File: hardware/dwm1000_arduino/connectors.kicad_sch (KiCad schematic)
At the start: 10 parts, among them J1 Barrel_Jack, J2 PWR_IN, J3 UART, J4 SPI, J5 NEO_OUT, J6 Conn_01x06_Male

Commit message: finixh schematic and first pass layout
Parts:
- removed J1: Barrel_Jack, symbol Connector:Barrel_Jack
- removed J2: PWR_IN, symbol Connector:Screw_Terminal_01x03
- added J1: RAW_PWR, TerminalBlock_Phoenix:TerminalBlock_Phoenix_PT-1,5-2-3.5-H_1x02_P3.50mm_Horizontal, symbol Connector:Screw_Terminal_01x02
- added J2: PWR_IN, TerminalBlock_Phoenix:TerminalBlock_Phoenix_PT-1,5-4-3.5-H_1x04_P3.50mm_Horizontal, symbol Connector:Screw_Terminal_01x04
- F1, F2: footprint (none) -> Fuse:Fuse_1206_3216Metric_Pad1.42x1.75mm_HandSolder; DigiKey (none) -> 507-1802-6-ND
- J3, J4: footprint (none) -> TerminalBlock_Phoenix:TerminalBlock_Phoenix_PT-1,5-4-3.5-H_1x04_P3.50mm_Horizontal; DigiKey (none) -> 277-1860-ND
- J5: footprint (none) -> Connector_PinHeader_2.54mm:PinHeader_1x03_P2.54mm_Vertical
- J6: value Conn_01x06_Male -> DEBUG; footprint (none) -> Connector_PinHeader_2.54mm:PinHeader_1x06_P2.54mm_Vertical
- TP1, TP2: footprint (none) -> TestPoint:TestPoint_Pad_D2.5mm
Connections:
- net ARD_RX: now also J3.2 (Pin_2); no longer J3.1 (Pin_1)
- net ARD_TX: now also J3.1 (Pin_1); no longer J3.2 (Pin_2)
- net GND: now also J1.1 (Pin_1), J2.1 (Pin_1), J2.2 (Pin_2)
- net SPI_MISO: now also J4.4 (Pin_4); no longer J4.3 (Pin_3)
- net SPI_MOSI: now also J4.3 (Pin_3); no longer J4.4 (Pin_4)
- net VCC: now also J1.2 (Pin_2)
- net at F2.1: now also J2.3 (Pin_3)
- net at F1.1: now also J2.4 (Pin_4)

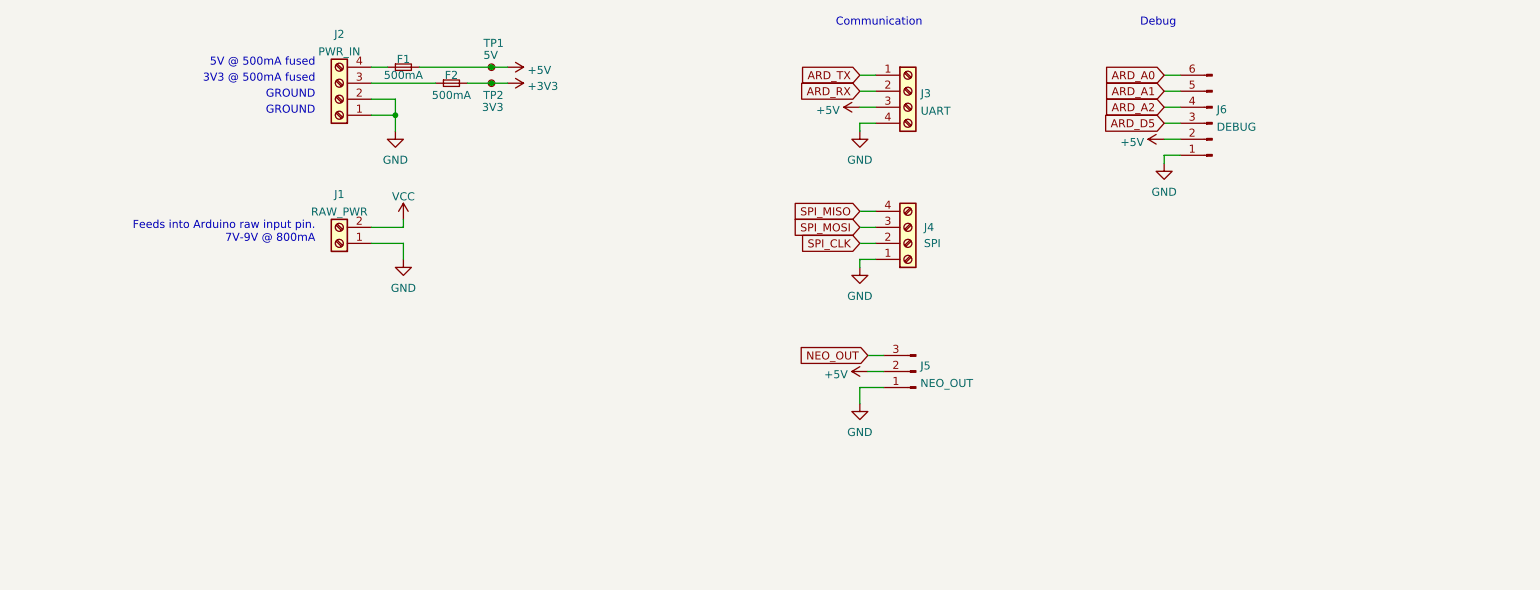
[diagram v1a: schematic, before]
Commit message: start rev 2 of the dwm board
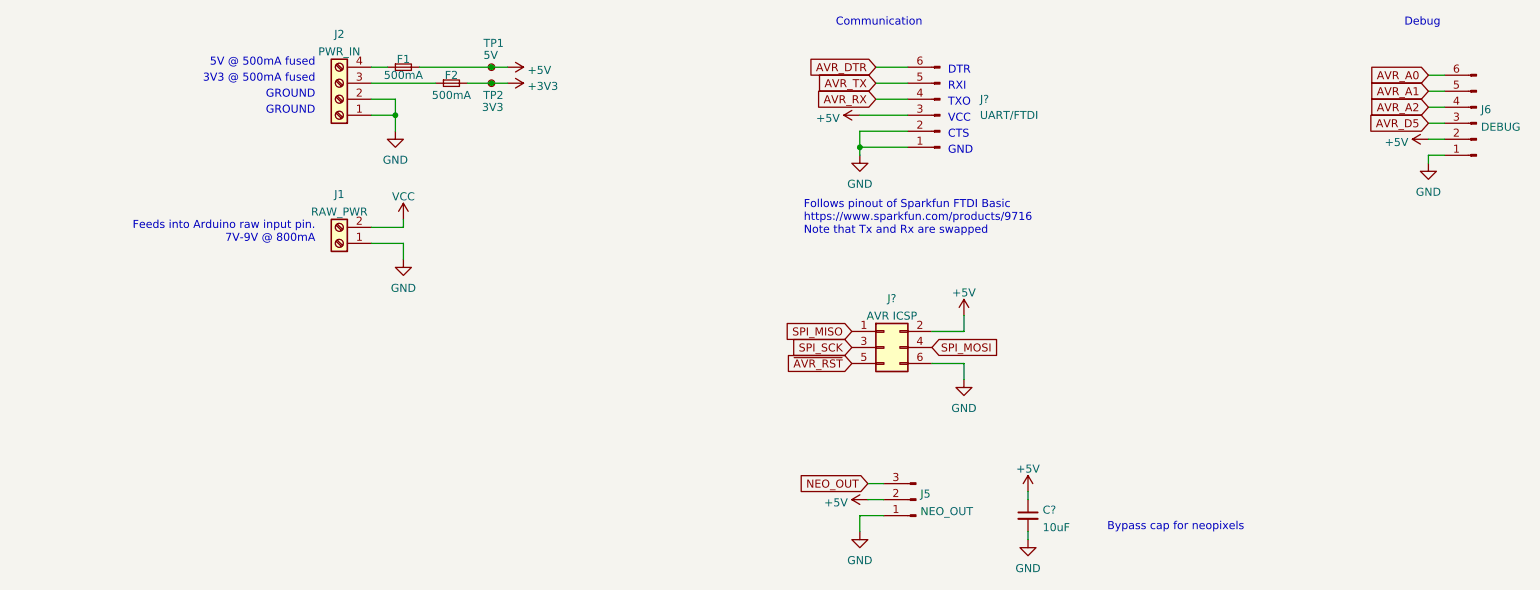
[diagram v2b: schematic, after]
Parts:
- removed J3: UART, TerminalBlock_Phoenix:TerminalBlock_Phoenix_PT-1,5-4-3.5-H_1x04_P3.50mm_Horizontal, symbol Connector:Screw_Terminal_01x04
- removed J4: SPI, TerminalBlock_Phoenix:TerminalBlock_Phoenix_PT-1,5-4-3.5-H_1x04_P3.50mm_Horizontal, symbol Connector:Screw_Terminal_01x04
- added C?: 10uF, Capacitor_SMD:C_0805_2012Metric_Pad1.18x1.45mm_HandSolder, symbol Device:C_Small
- added J?: UART/FTDI, Connector_PinHeader_2.54mm:PinHeader_1x06_P2.54mm_Vertical, symbol Connector:Conn_01x06_Male
- added J?: AVR ICSP, symbol Connector_Generic:Conn_02x03_Odd_Even
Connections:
- net +5V: now also C?.1, J?.2 (Pin_2), J?.3 (Pin_3)
- net GND: now also C?.2, J?.1 (Pin_1), J?.2 (Pin_2), J?.6 (Pin_6)
- net SPI_MISO: now also J?.1 (Pin_1)
- net SPI_MOSI: now also J?.4 (Pin_4)
- net ARD_A0 renamed AVR_A0
- net ARD_A1 renamed AVR_A1
- net ARD_A2 renamed AVR_A2
- net ARD_D5 renamed AVR_D5
- new net AVR_DTR: J?.6 (Pin_6)
- new net AVR_RX: J?.4 (Pin_4)
- new net AVR_TX: J?.5 (Pin_5)
- new net SPI_SCK: J?.3 (Pin_3)
- new net ~{AVR_RST}: J?.5 (Pin_5)
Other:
- note added: "Bypass cap for neopixels"
- note added: "CTS"
- note added: "DTR"
- note added: "Follows pinout of Sparkfun FTDI Basic https://www.sparkfun.com/products/9716 Note that Tx and Rx are swapped"
- note added: "GND"
- note added: "RXI"
- note added: "TXO"
- note added: "VCC"
- moved on the sheet: J5, J6

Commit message: rev 2 pcb schematic
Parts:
- gave numbers to parts that had none: 3
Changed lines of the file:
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@@
   (symbol (lib_id "power:GND") (at 199.39 148.59 0) (unit 1)
     (in_bom yes) (on_board yes) (fields_autoplaced)
-    (property "Reference" "#PWR?" (id 0) (at 199.39 154.94 0)
+    (property "Reference" "#PWR044" (id 0) (at 199.39 154.94 0)
       (effects (font (size 1.27 1.27)) hide)
     )
@@
   (symbol (lib_id "power:+5V") (at 199.39 138.43 0) (unit 1)
     (in_bom yes) (on_board yes) (fields_autoplaced)
-    (property "Reference" "#PWR?" (id 0) (at 199.39 142.24 0)
+    (property "Reference" "#PWR043" (id 0) (at 199.39 142.24 0)
       (effects (font (size 1.27 1.27)) hide)
     )
@@
   (symbol (lib_id "Connector:Conn_01x06_Male") (at 195.58 106.68 180) (unit 1)
     (in_bom yes) (on_board yes)
-    (property "Reference" "J?" (id 0) (at 201.93 104.14 0)
+    (property "Reference" "J4" (id 0) (at 201.93 104.14 0)
       (effects (font (size 1.27 1.27)) (justify right))
     )
@@
   (symbol (lib_id "power:+5V") (at 209.55 166.37 0) (unit 1)
     (in_bom yes) (on_board yes) (fields_autoplaced)
-    (property "Reference" "#PWR?" (id 0) (at 209.55 170.18 0)
+    (property "Reference" "#PWR045" (id 0) (at 209.55 170.18 0)
       (effects (font (size 1.27 1.27)) hide)
     )
@@
   (symbol (lib_id "Device:C_Small") (at 209.55 170.18 0) (unit 1)
     (in_bom yes) (on_board yes) (fields_autoplaced)
-    (property "Reference" "C?" (id 0) (at 211.8741 169.2778 0)
+    (property "Reference" "C15" (id 0) (at 211.8741 169.2778 0)
       (effects (font (size 1.27 1.27)) (justify left))
     )
@@
   (symbol (lib_id "power:GND") (at 209.55 173.99 0) (unit 1)
     (in_bom yes) (on_board yes) (fields_autoplaced)
-    (property "Reference" "#PWR?" (id 0) (at 209.55 180.34 0)
+    (property "Reference" "#PWR046" (id 0) (at 209.55 180.34 0)
       (effects (font (size 1.27 1.27)) hide)
     )
@@
   (symbol (lib_id "Connector_Generic:Conn_02x03_Odd_Even") (at 186.69 143.51 0) (unit 1)
     (in_bom yes) (on_board yes) (fields_autoplaced)
-    (property "Reference" "J?" (id 0) (at 187.96 135.7335 0))
+    (property "Reference" "J3" (id 0) (at 187.96 135.7335 0))
     (property "Value" "AVR ICSP" (id 1) (at 187.96 138.5086 0))
     (property "Footprint" "" (id 2) (at 186.69 143.51 0)

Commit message: finish layout
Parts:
- J2: value PWR_IN -> PWR_OUT
- J3: footprint (none) -> Connector_PinHeader_2.54mm:PinHeader_2x03_P2.54mm_Vertical
- TP1, TP2: footprint TestPoint:TestPoint_Pad_D2.5mm -> TestPoint:TestPoint_Pad_D1.0mm
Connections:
- net NEO_OUT renamed NEO_DATA
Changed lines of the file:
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@@
     (effects (font (size 1.27 1.27)) (justify left bottom))
   )
-  (global_label "NEO_OUT" (shape input) (at 184.15 165.1 180) (fields_autoplaced)
-    (effects (font (size 1.27 1.27)) (justify right))
-    (property "Intersheet References" "${INTERSHEET_REFS}" (id 0) (at 173.3307 165.0206 0)
+  (global_label "NEO_DATA" (shape input) (at 184.15 165.1 180) (fields_autoplaced)
+    (effects (font (size 1.27 1.27)) (justify right))
+    (property "Intersheet References" "${INTERSHEET_REFS}" (id 0) (at 172.5445 165.0206 0)
       (effects (font (size 1.27 1.27)) (justify right) hide)
     )
@@
     (in_bom yes) (on_board yes) (fields_autoplaced)
     (property "Reference" "J2" (id 0) (at 100.33 93.8235 0))
-    (property "Value" "PWR_IN" (id 1) (at 100.33 96.5986 0))
+    (property "Value" "PWR_OUT" (id 1) (at 100.33 96.5986 0))
     (property "Footprint" "TerminalBlock_Phoenix:TerminalBlock_Phoenix_PT-1,5-4-3.5-H_1x04_P3.50mm_Horizontal" (id 2) (at 100.33 104.14 0)
       (effects (font (size 1.27 1.27)) hide)
@@
       (effects (font (size 1.27 1.27)) (justify left))
     )
-    (property "Footprint" "TestPoint:TestPoint_Pad_D2.5mm" (id 2) (at 119.38 101.6 0)
+    (property "Footprint" "TestPoint:TestPoint_Pad_D1.0mm" (id 2) (at 119.38 101.6 0)
       (effects (font (size 1.27 1.27)) hide)
     )
@@
     (property "Reference" "J3" (id 0) (at 187.96 135.7335 0))
     (property "Value" "AVR ICSP" (id 1) (at 187.96 138.5086 0))
-    (property "Footprint" "" (id 2) (at 186.69 143.51 0)
+    (property "Footprint" "Connector_PinHeader_2.54mm:PinHeader_2x03_P2.54mm_Vertical" (id 2) (at 186.69 143.51 0)
       (effects (font (size 1.27 1.27)) hide)
     )
@@
       (effects (font (size 1.27 1.27)) (justify left))
     )
-    (property "Footprint" "TestPoint:TestPoint_Pad_D2.5mm" (id 2) (at 129.54 99.06 0)
-      (effects (font (size 1.27 1.27)) hide)
-    )
+    (property "Footprint" "TestPoint:TestPoint_Pad_D1.0mm" (id 2) (at 129.54 99.06 0)
+      (effects (font (size 1.27 1.27)) hide)
+    )
